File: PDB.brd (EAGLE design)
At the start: 159.7 x 151.3 mm, 77 parts, among them IC1 LM555N

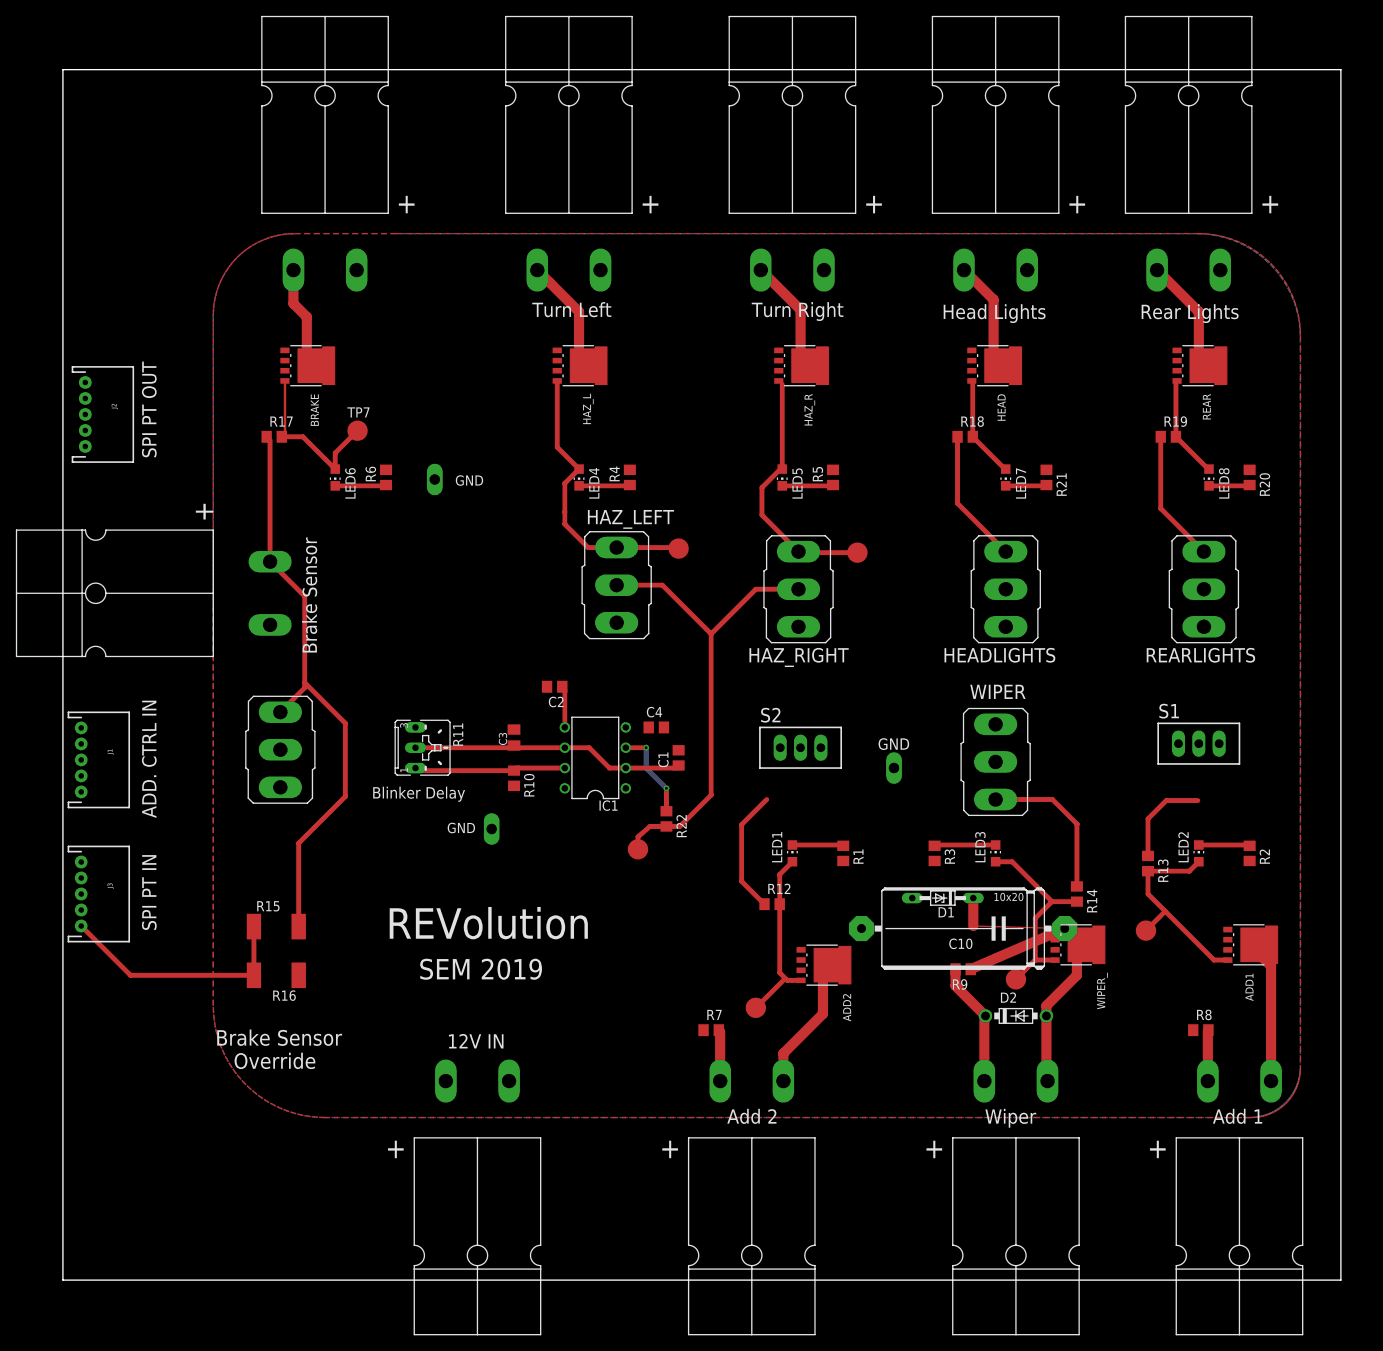
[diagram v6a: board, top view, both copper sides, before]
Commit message: changed a lot of routing, near final version with JSTs
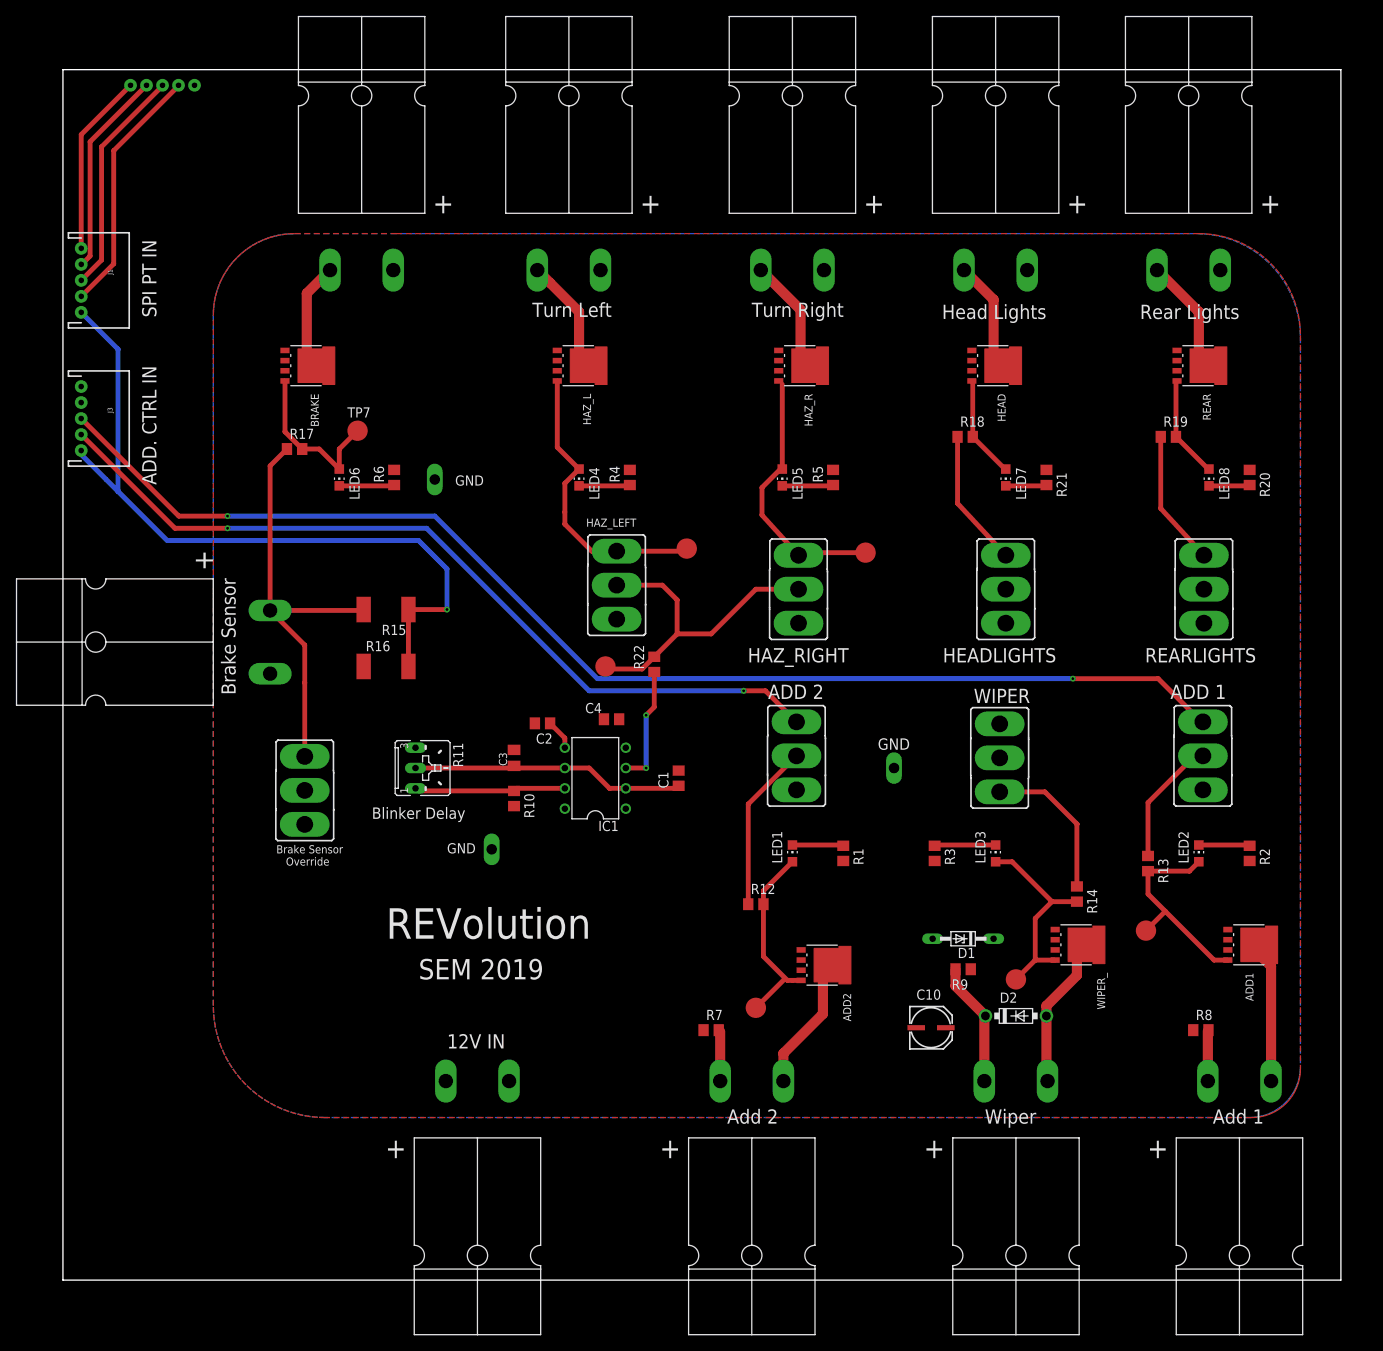
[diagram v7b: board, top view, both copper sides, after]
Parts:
- removed S1, S2: TL39PO, switch:TL3XPO
- added ADD1_, ADD2_: (no value), switch:M9040P
- C10: value (none) -> 22uF; device resistor:EU25-10 -> SparkFun-Capacitors:PANASONIC_C
- moved J1 59.9 mm to (0.00, 102.1)
- moved J3 59.4 mm to (0.00, 84.8)
- moved J2 42.3 mm to (10.2, 126.5), flipped to the bottom, turned to 180 degrees
- moved R15 41.9 mm to (38.1, 61.0), turned to 180 degrees
- moved R16 41.0 mm to (38.1, 53.8), turned to 0 degrees
- moved TP1 23.2 mm to (65.5, 53.8)
- moved R22 19.4 mm to (71.6, 54.1), turned to 90 degrees
- moved C10 12.9 mm to (106.2, 8.89), turned to 0 degrees
- moved VDD_IN1 6.10 mm to (16.5, 56.9)
- moved BRAKE_SNS_OVR 5.92 mm to (27.9, 38.4)
- moved C4 5.68 mm to (66.3, 47.2)
- moved D1 5.68 mm to (110.2, 19.8)
- moved C2 4.82 mm to (57.7, 46.7)
- moved BRAKE_OUT 4.57 mm to (35.1, 110.5)
- moved R17 2.96 mm to (26.7, 81.0)
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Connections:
- net GND: now also C10.-; no longer C10.2
- net H5: now also ADD1_.2; no longer S1.2
- net H6: now also ADD2_.2; no longer S2.2
- net VDD: now also ADD1_.3, ADD2_.3, C10.+; no longer C10.1, S1.3, S2.3
- net µC_1: now also ADD1_.1; no longer S1.1
- net µC_2: now also ADD2_.1; no longer S2.1
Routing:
- net µC_1: track 0.00 -> 155.9 mm, vias 0 -> 2
- net µC_2: track 0.00 -> 104.3 mm, vias 0 -> 2
- net BRK_SNS_5V: track 30.2 -> 93.4 mm, vias 0 -> 1
- net MISO_SPI: track 0.00 -> 31.4 mm
- net MOSI_SPI: track 0.00 -> 28.6 mm
- net VDD: track 27.7 -> 0.00 mm
- net CS_SPI: track 0.00 -> 25.8 mm
- net SCL_SPI: track 0.00 -> 22.9 mm
- net BRAKE_SNS_: track 72.7 -> 53.1 mm
- net 555_OUT: track 60.5 -> 41.2 mm
- net H6: track 15.6 -> 21.0 mm
- net H5: track 12.3 -> 16.5 mm
- net Q: track 11.5 -> 15.0 mm
- net N$7: track 23.6 -> 25.3 mm
- net H2: track 32.1 -> 33.6 mm
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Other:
- board text added: "ADD 1"
- board text added: "ADD 2"

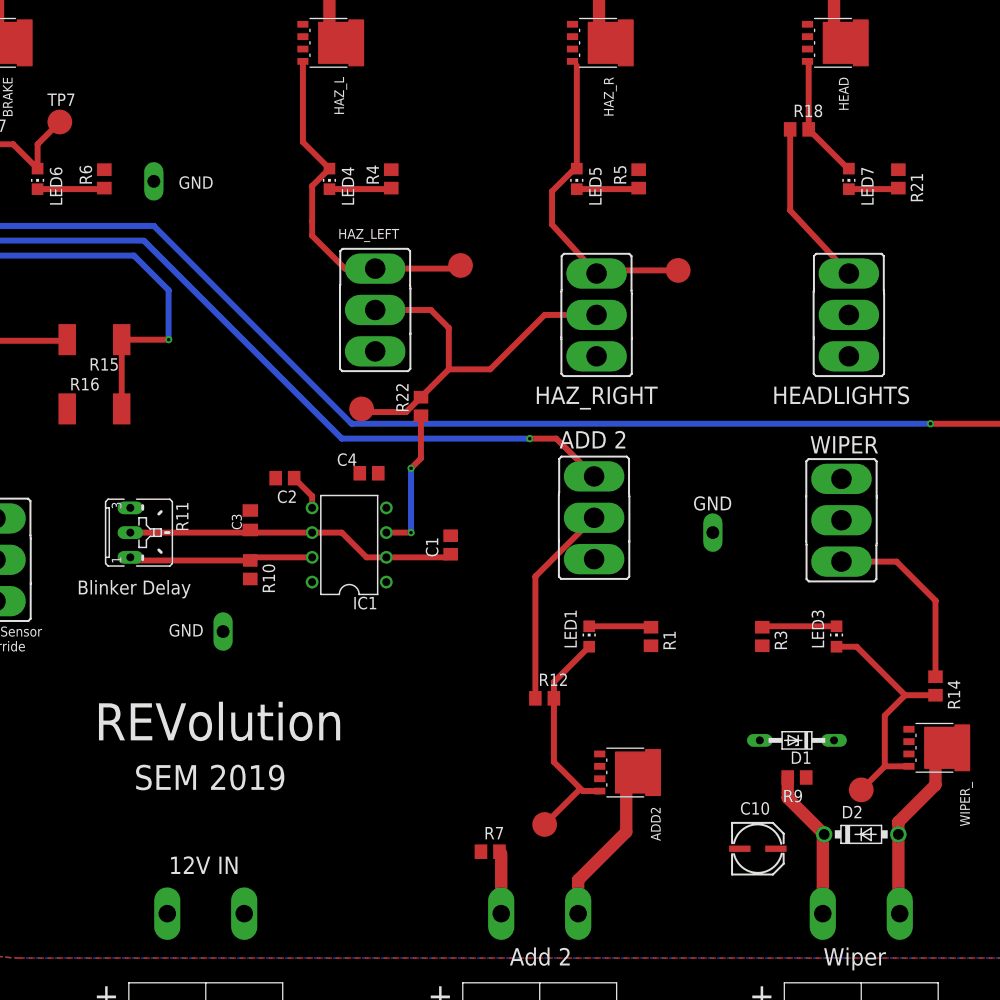
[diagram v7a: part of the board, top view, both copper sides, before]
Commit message: updated PDB board
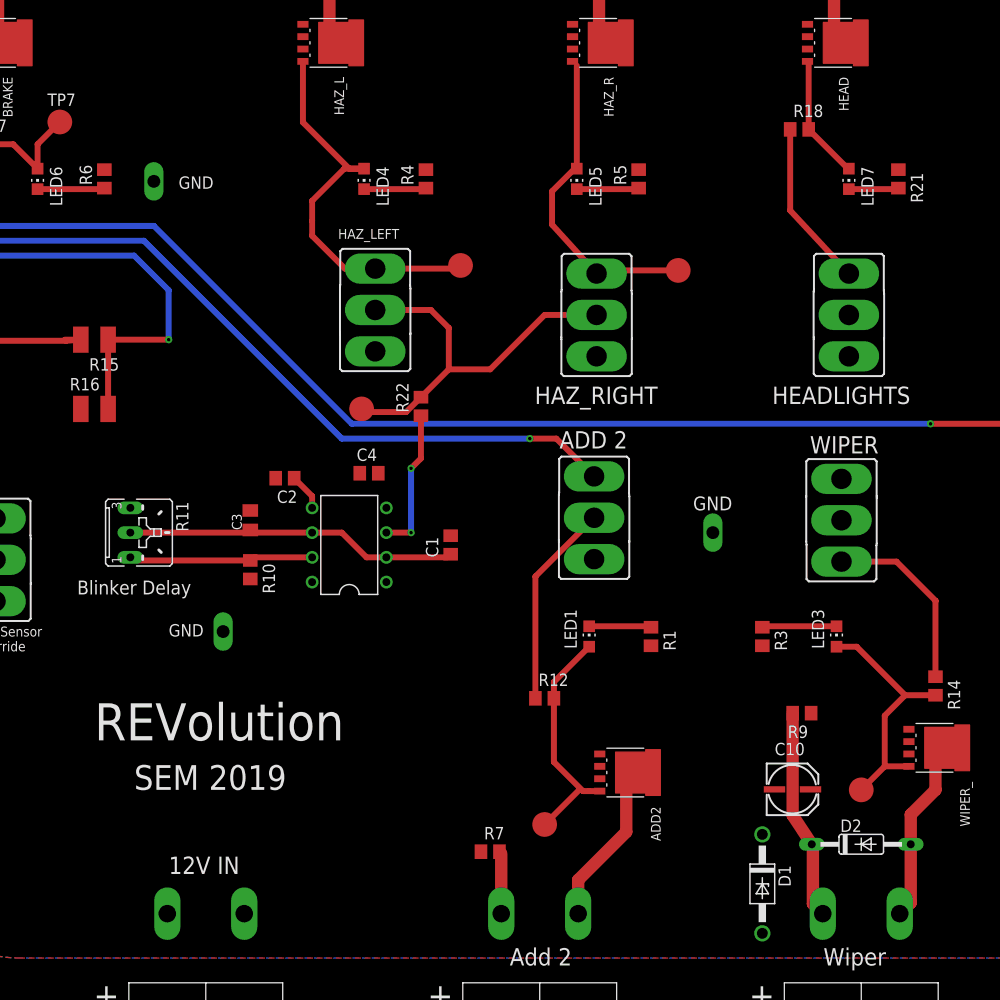
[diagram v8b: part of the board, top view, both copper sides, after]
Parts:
- D1: device diode:DO34Z7 -> diode:DO41Z10
- D2: value 1N5817-B -> 1N4446; device diode:DO41-7.6 -> diode:DO35-10
- R1, R2, R20, R21, R3, R4, R5, R6: value 10K -> 510
- R15, R16: device resistor:R2512 -> resistor:R3225
- moved D1 15.2 mm to (106.7, 5.08), turned to 270 degrees
- moved C10 7.06 mm to (109.7, 15.0)
- moved R9 6.62 mm to (110.7, 22.6)
- moved LED4 3.56 mm to (65.8, 77.5)
- moved R4 3.56 mm to (72.1, 77.5)
- moved D2 1.02 mm to (116.8, 9.14)
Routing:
- net N$20: track 15.6 -> 21.7 mm
- net H3: track 36.6 -> 41.6 mm
- net BRAKE_SNS_: track 53.1 -> 55.8 mm
- net BRK_SNS_5V: track 93.4 -> 94.8 mm
